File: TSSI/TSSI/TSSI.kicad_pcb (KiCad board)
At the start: 2 copper layers, 42 x 41.5 mm, 23 parts, among them J1 Conn_01x03_Socket, J2 B2P-VHLFSN, J3 B2P-VHLFSN, J4 B2P-VHLFSN, J5 B2P-VHLFSN, J6 B4P-VH, U1 ATtiny1614-SS, U2 MCP1703T-5002E/CB

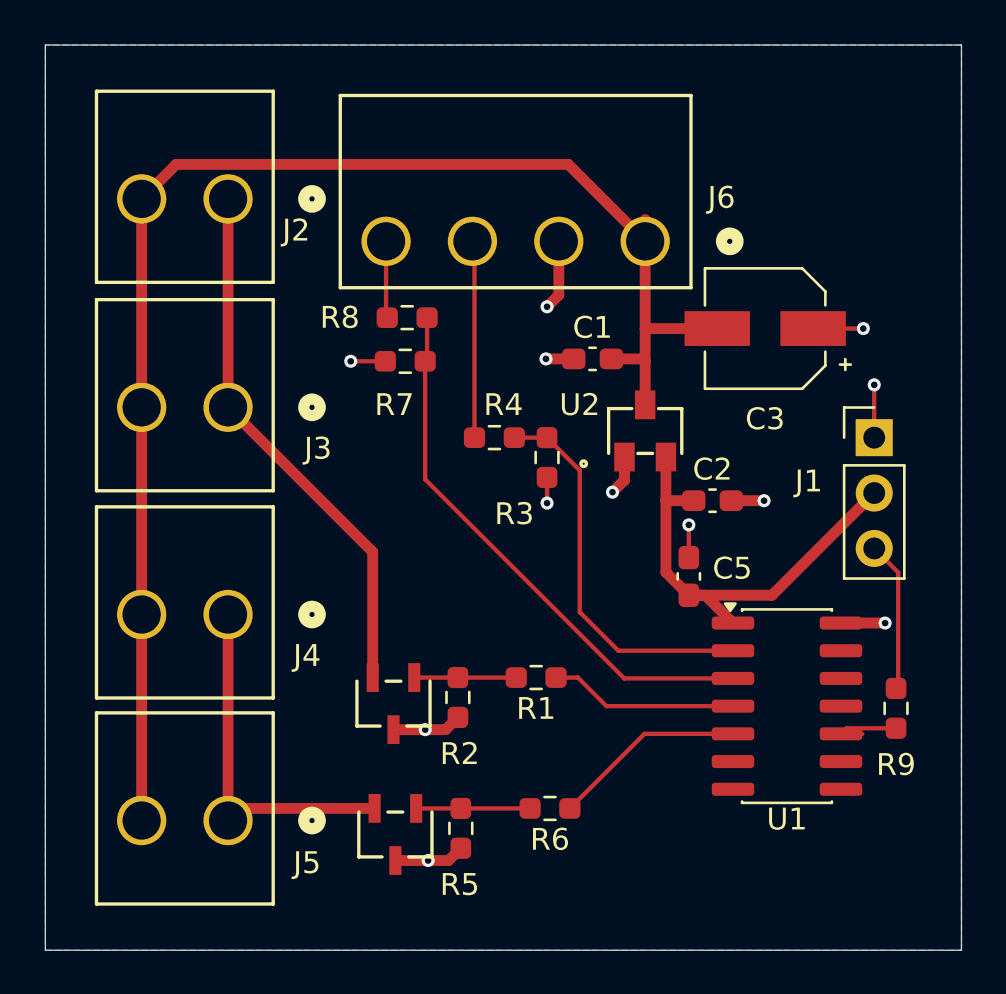
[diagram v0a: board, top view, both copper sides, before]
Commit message: Changed chematic for cleanliness and some standardization issues
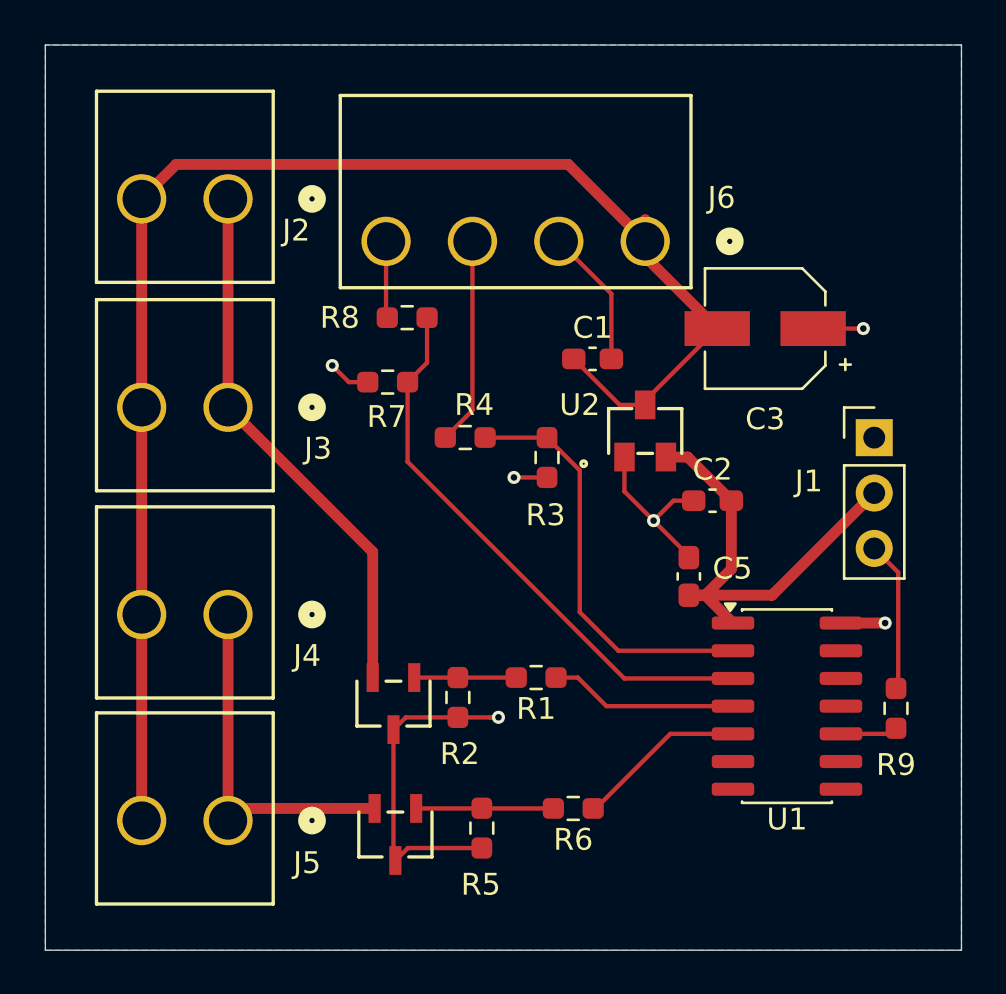
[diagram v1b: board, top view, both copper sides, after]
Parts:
- moved R4 1.34 mm to (150.7, 87.0)
- moved R7 1.25 mm to (147.2, 84.5)
- moved R6 1.07 mm to (155.7, 104.0)
- moved R5 0.96 mm to (151.5, 104.9)
- renumbered Mosfet1 to Q1, Mosfet2 to Q2
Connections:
- C1 pad 1: GNDREF -> +12V
- C1 pad 2: +12V -> GND
- C2 pad 1: +5V -> GND
- C2 pad 2: GNDREF -> +5V
- C3 pad 1: GNDREF -> GND
- C5 pad 2: GNDREF -> GND
- J1 pad 1: GNDREF -> GND
- J6 pad 2: GNDREF -> GND
- Q1 pad 3: GNDREF -> GND
- Q2 pad 3: GNDREF -> GND
- R2 pad 1: GNDREF -> GND
- R3 pad 1: GNDREF -> GND
- R5 pad 1: GNDREF -> GND
- R7 pad 1: GNDREF -> GND
- U1 pad 14: GNDREF -> GND
- U2 pad 1: GNDREF -> GND
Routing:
- net GND: track 0.00 -> 37.7 mm, vias 0 -> 6
- net GNDREF: track 25.3 -> 0.00 mm, vias 12 -> 0
- net +12V: track 67.1 -> 69.1 mm
- net Net-(U1-PA4): track 17.9 -> 19.2 mm
- net Net-(Q2-G): track 5.22 -> 6.30 mm
- net GRN: track 8.89 -> 7.83 mm
- net Net-(U1-~{RESET}/PA0): track 3.61 -> 2.63 mm
- net Net-(U1-PA5): track 25.3 -> 26.0 mm
- net +5V: track 21.0 -> 21.7 mm
- added copper zone on B.Cu, net GND
- removed copper zone on B.Cu, net GNDREF

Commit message: Changed resistor divider and trimmed board dimensions
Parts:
- R3, R7: value 4.7K -> 6.8k
- moved C3 7.50 mm to (167.9, 75.3)
- moved U2 4.95 mm to (162.9, 83.7)
- moved R9 4.89 mm to (171.4, 94.6)
- moved J1 4.22 mm to (169.9, 82.8)
- moved R1 3.95 mm to (153.6, 94.1)
- moved R5 3.95 mm to (151.1, 101.0)
- moved R6 3.95 mm to (155.3, 100.1)
- moved Q1 3.95 mm to (147.0, 95.3)
- moved Q2 3.95 mm to (147.1, 101.3)
- moved R2 3.95 mm to (150.0, 95.0)
- moved U1 3.73 mm to (166.1, 95.6)
- moved C5 3.14 mm to (158.6, 91.3)
- moved C2 2.23 mm to (163.1, 87.9)
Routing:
- net GND: track 37.7 -> 48.1 mm, vias 6 -> 4
- net +12V: track 69.1 -> 77.9 mm
- net Net-(Q1-D): track 24.7 -> 20.6 mm
- net +5V: track 21.7 -> 18.5 mm
- net Net-(U1-PA4): track 19.2 -> 16.6 mm
- net Net-(Q2-D): track 16.4 -> 17.6 mm
- net RED: track 8.66 -> 9.79 mm
- net GRN: track 7.83 -> 8.88 mm
- net Net-(U1-PA5): track 26.0 -> 25.2 mm
- net Net-(U1-~{RESET}/PA0): track 2.63 -> 3.43 mm
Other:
- outline, holes or cut-outs redrawn
